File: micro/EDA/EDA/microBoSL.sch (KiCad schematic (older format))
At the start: 43 parts, among them J1 Conn_01x04, J2 Conn_01x03, J3 Conn_01x04, J4 BATTERY CONN, J5 Conn_02x03_Odd_Even, J6 Conn_01x04, J7 MOTOR_OUT, J8 USB_B_Micro, Q1 DMP2165UW, SW1 RST_JMPR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

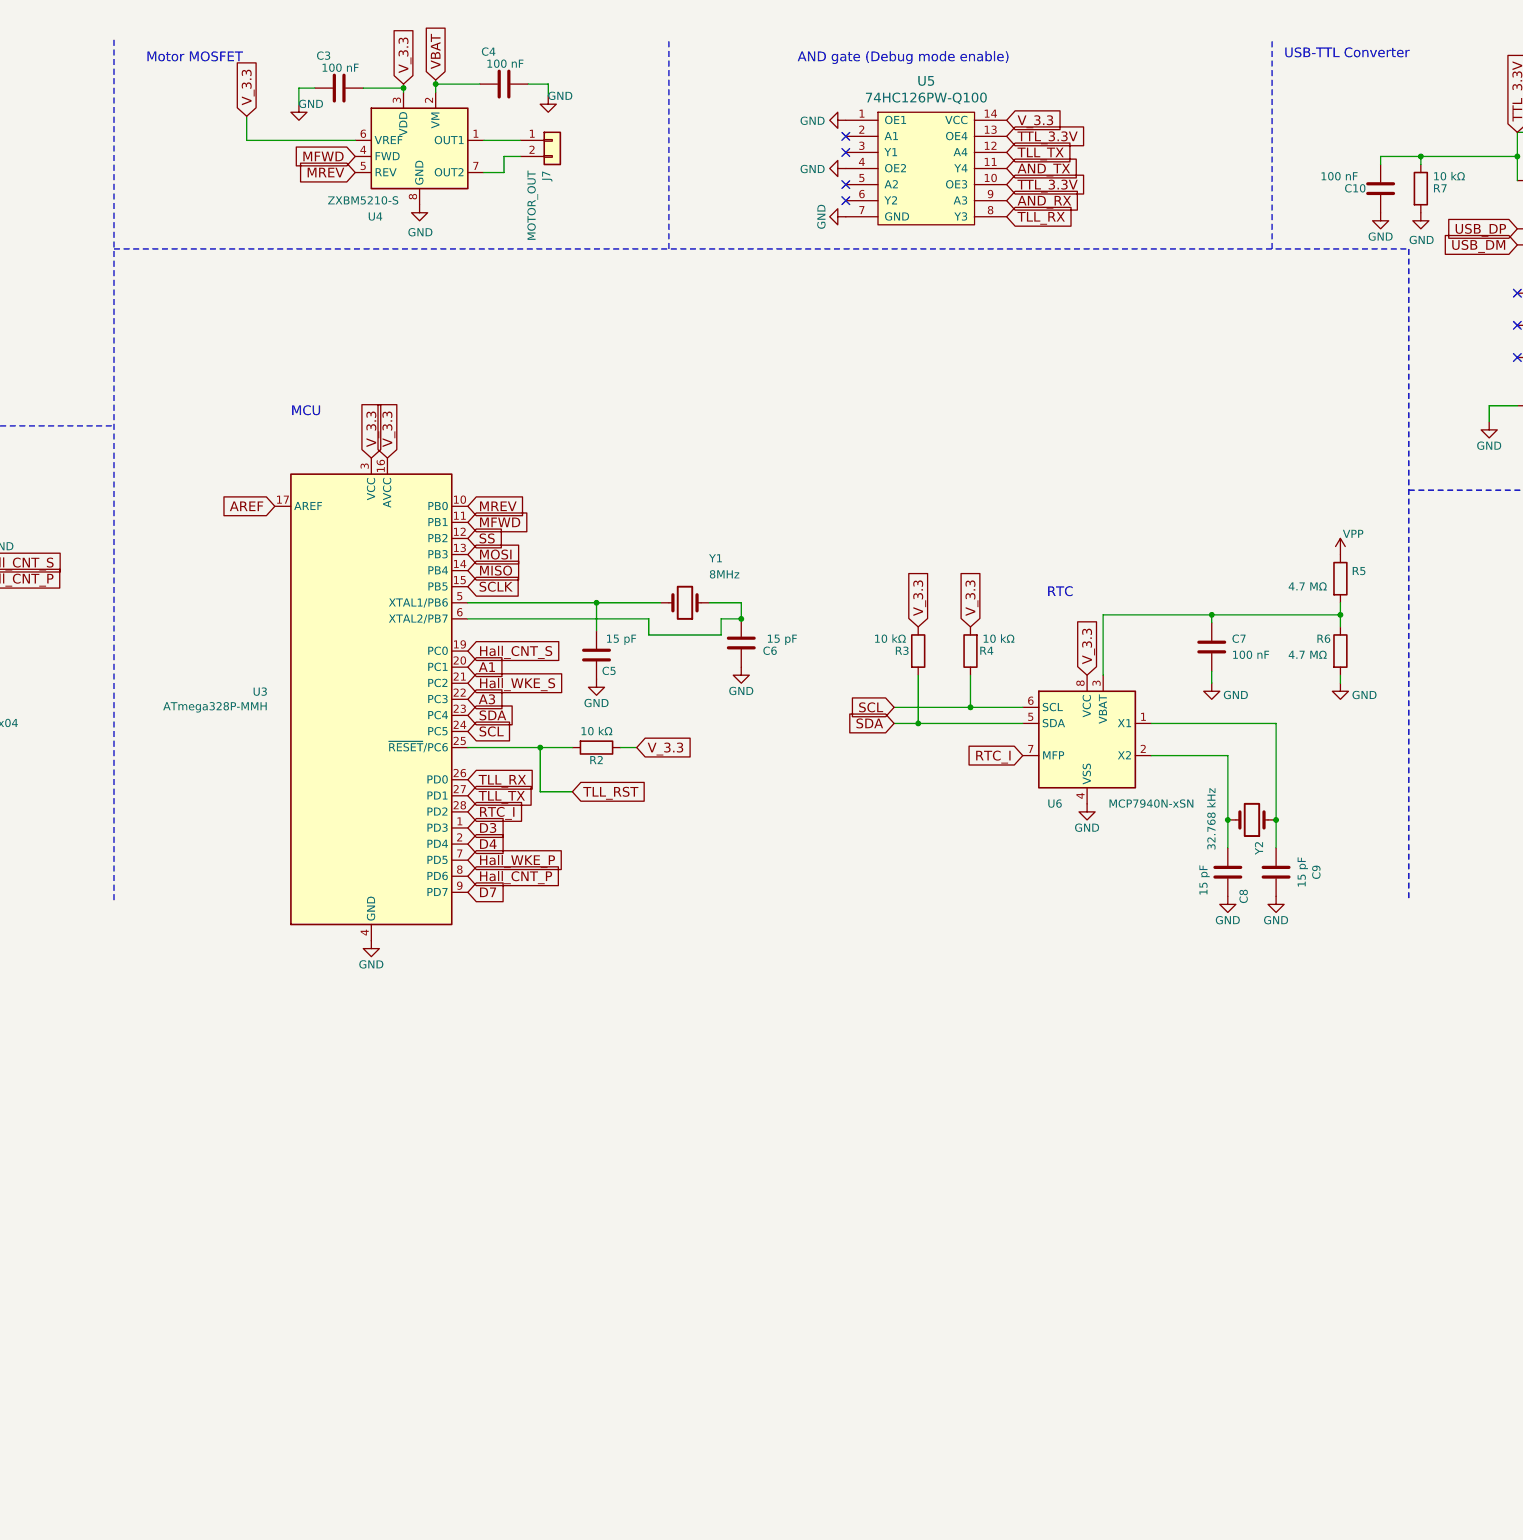
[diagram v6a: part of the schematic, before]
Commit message: added 3 motors to the microBoSL in schematic and PCB, traces and silkscreen still need optimising
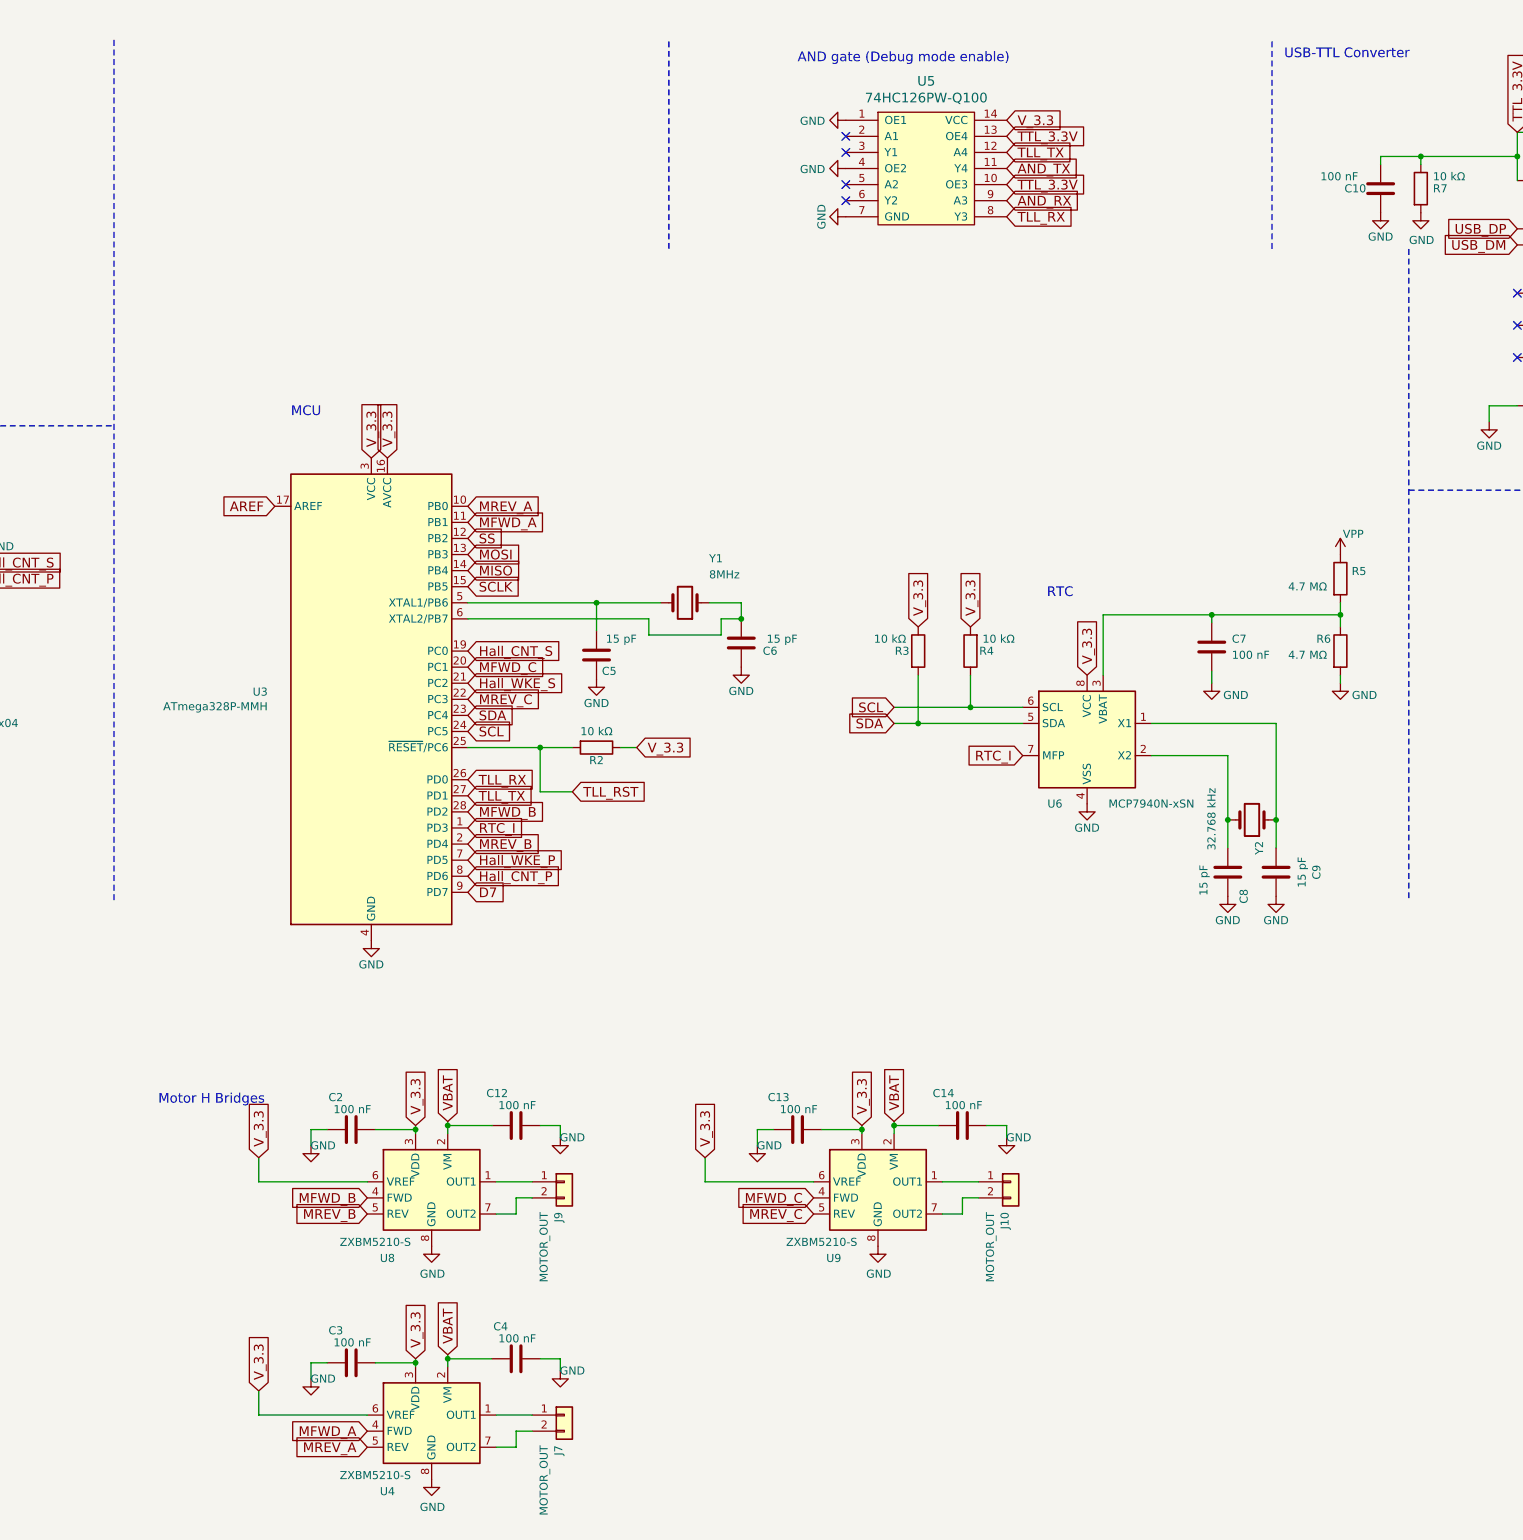
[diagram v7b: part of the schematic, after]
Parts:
- added C12, C13, C14, C2: 100 nF, Capacitor_SMD:C_0402_1005Metric, symbol Device:C
- added J10, J9: MOTOR_OUT, Connector_PinHeader_2.54mm:PinHeader_1x02_P2.54mm_Vertical, symbol Connector_Generic:Conn_01x02
- added U8, U9: ZXBM5210-S, Package_SO:SOIC-8_3.9x4.9mm_P1.27mm, symbol Driver_Motor:ZXBM5210-S
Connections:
- net D3 is gone; now on net RTC_I: U3.1 (PD3)
- net GND: now also C12.2, C13.1, C14.2, C2.1, U8.8 (GND), U9.8 (GND)
- net RTC_I: no longer U3.28 (PD2)
- net VBAT: now also C12.1, C14.1, U8.2 (VM), U9.2 (VM)
- net V_3.3: now also C13.2, C2.2, U8.3 (VDD), U8.6 (VREF), U9.3 (VDD), U9.6 (VREF)
- net A1 renamed MFWD_C
- net MFWD_C: now also U9.4 (FWD)
- net A3 renamed MREV_C
- net MREV_C: now also U9.5 (REV)
- net D4 renamed MREV_B
- net MREV_B: now also U8.5 (REV)
- net MFWD renamed MFWD_A
- net MREV renamed MREV_A
- new net: J9.1 (Pin_1), U8.1 (OUT1)
- new net: J9.2 (Pin_2), U8.7 (OUT2)
- new net: J10.1 (Pin_1), U9.1 (OUT1)
- new net: J10.2 (Pin_2), U9.7 (OUT2)
- new net MFWD_B: U3.28 (PD2), U8.4 (FWD)
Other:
- note added: "Motor H Bridges"
- note removed: "Motor MOSFET"
- moved on the sheet: C3, C4, J7, U4
